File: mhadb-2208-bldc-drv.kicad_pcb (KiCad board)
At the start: 2 copper layers, 45 x 40 mm, 69 parts, among them J1 TC2030, J2 Conn_01x04, J3 Conn_01x04_Pin, M1 Motor_3_Phases, SW1 SW_Push, SW2 SW_Push, SW3 SW_Push, U1 SN65HVD230, U2 STM32F103C8Tx, U3 DRV8311H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

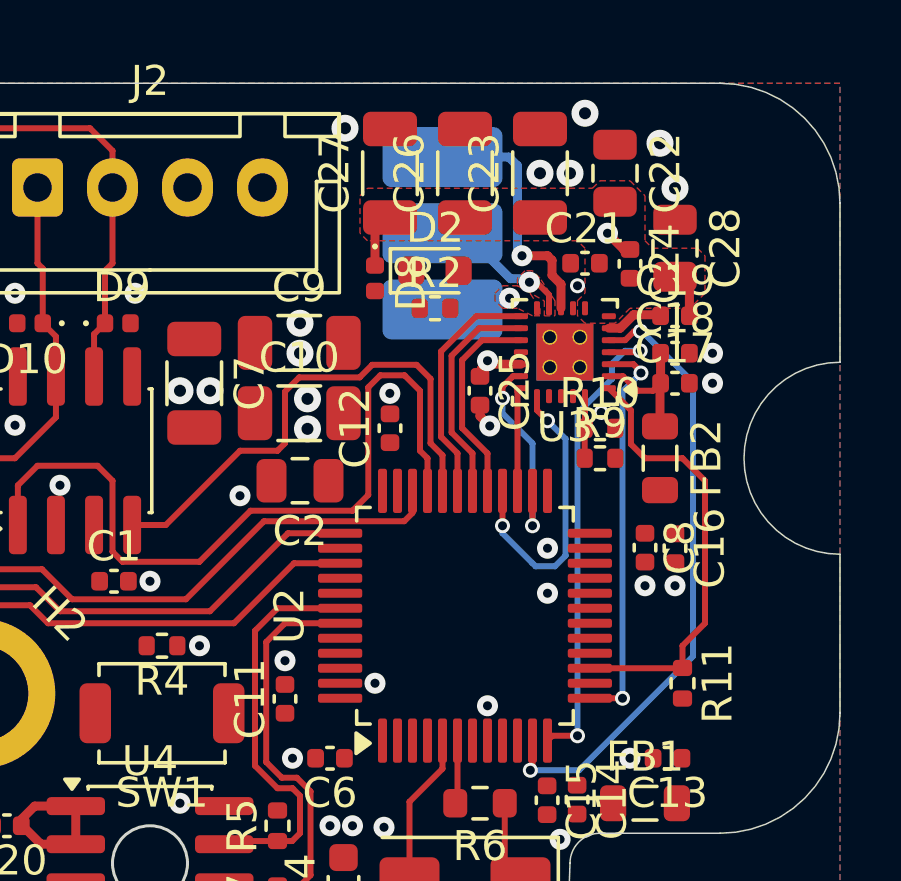
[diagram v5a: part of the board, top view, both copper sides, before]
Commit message: pcb: route +BATT power
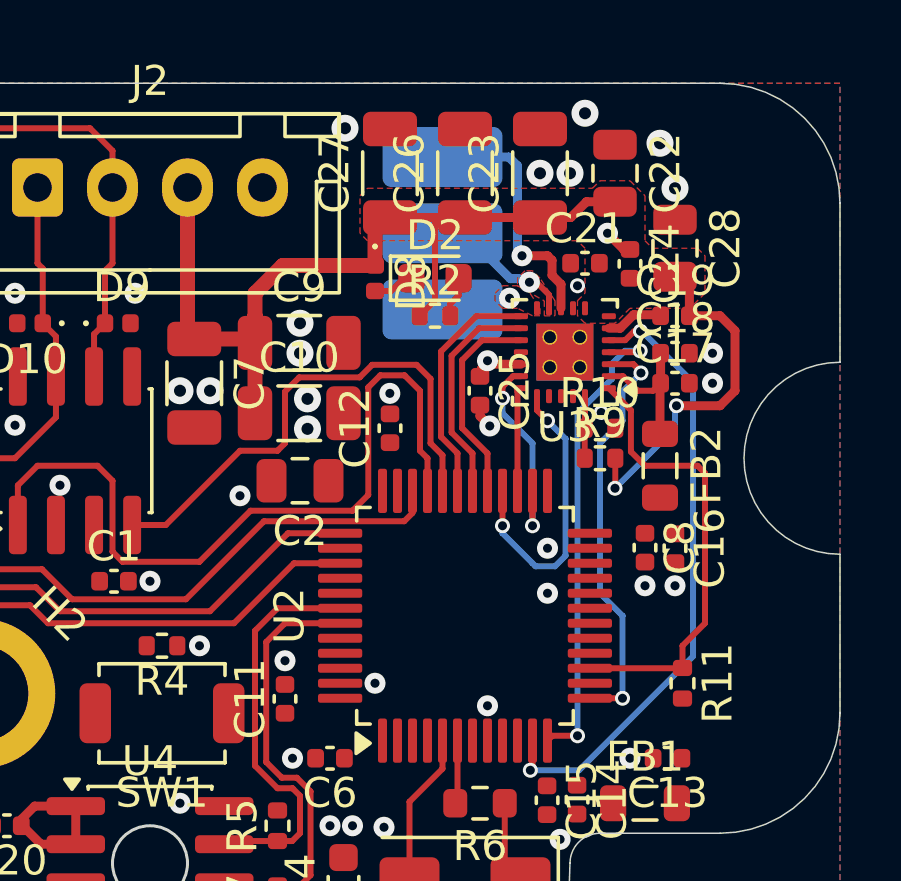
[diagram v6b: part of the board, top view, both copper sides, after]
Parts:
- moved D2 0.25 mm to (128.5, 66.5)
- moved FB2 0.25 mm to (136.0, 72.8)
- moved R2 0.25 mm to (128.5, 67.8)
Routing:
- net +BATT: track 3.31 -> 40.6 mm, vias 0 -> 2
- net GND: track 1.80 -> 3.29 mm
- net Net-(D2-A): track 0.00 -> 1.36 mm
- net /SOC: track 13.4 -> 14.0 mm

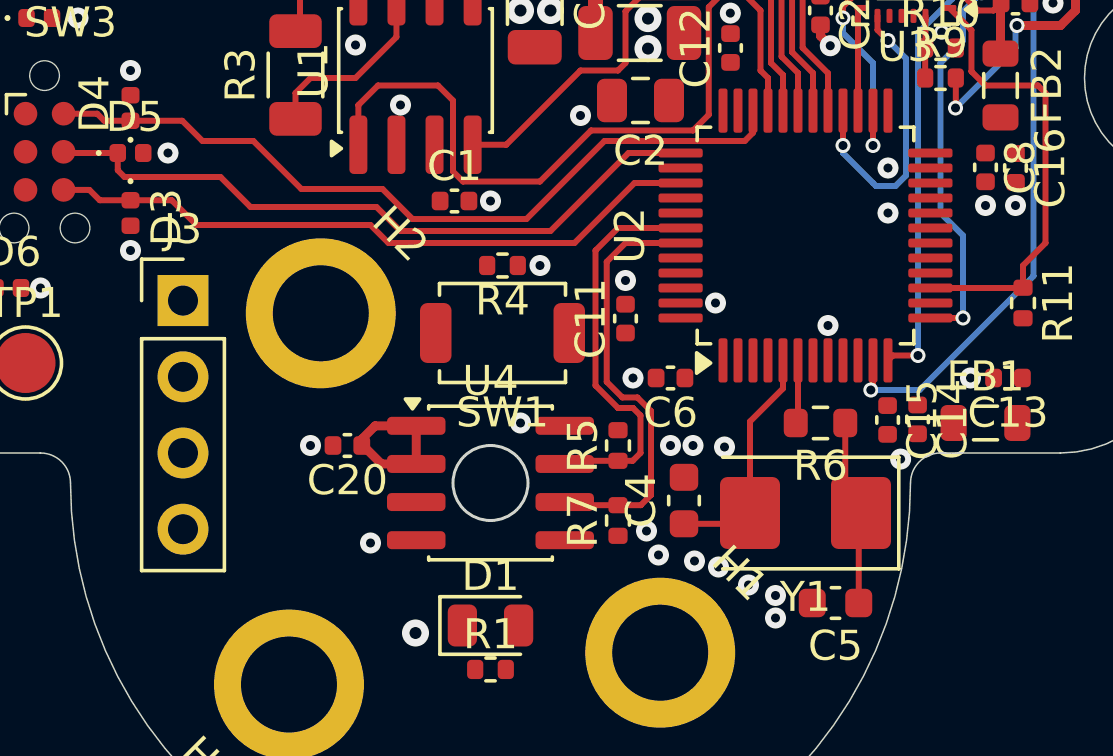
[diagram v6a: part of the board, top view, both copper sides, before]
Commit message: pcb: route spare GPIOs
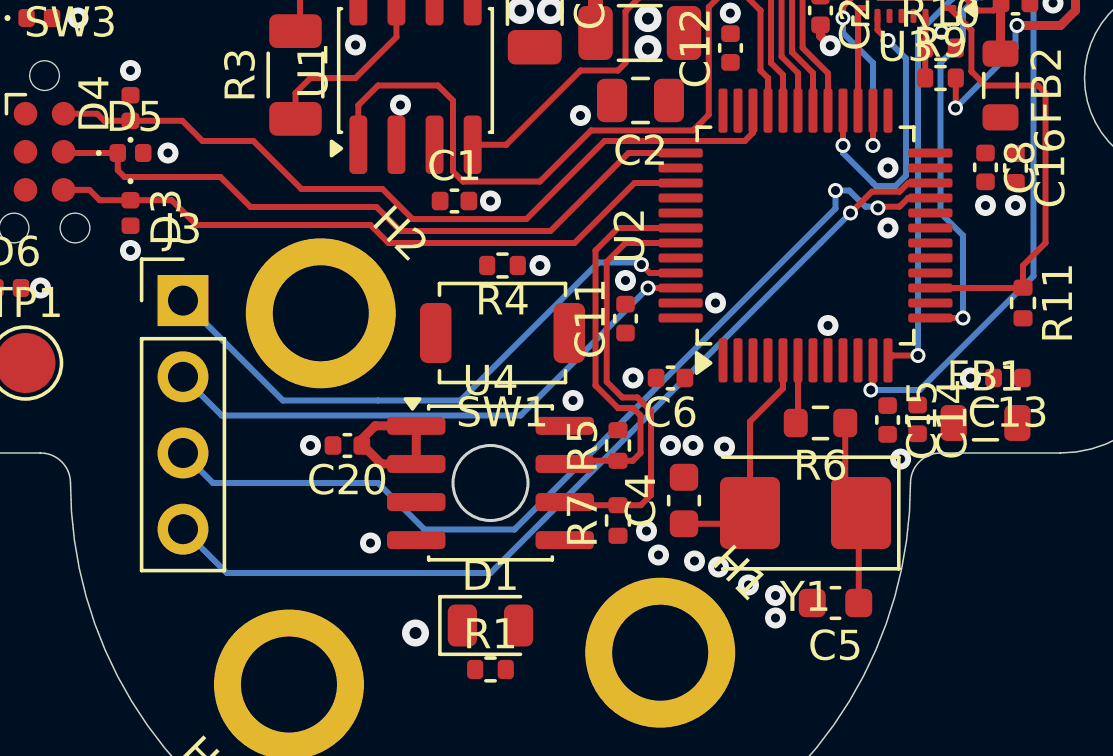
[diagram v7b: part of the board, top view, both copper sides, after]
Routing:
- net Net-(J3-Pin_3): track 0.00 -> 31.4 mm, vias 0 -> 2
- net Net-(J3-Pin_4): track 0.00 -> 30.9 mm, vias 0 -> 1
- net Net-(J3-Pin_1): track 0.00 -> 20.0 mm, vias 0 -> 1
- net Net-(J3-Pin_2): track 0.00 -> 18.9 mm, vias 0 -> 1

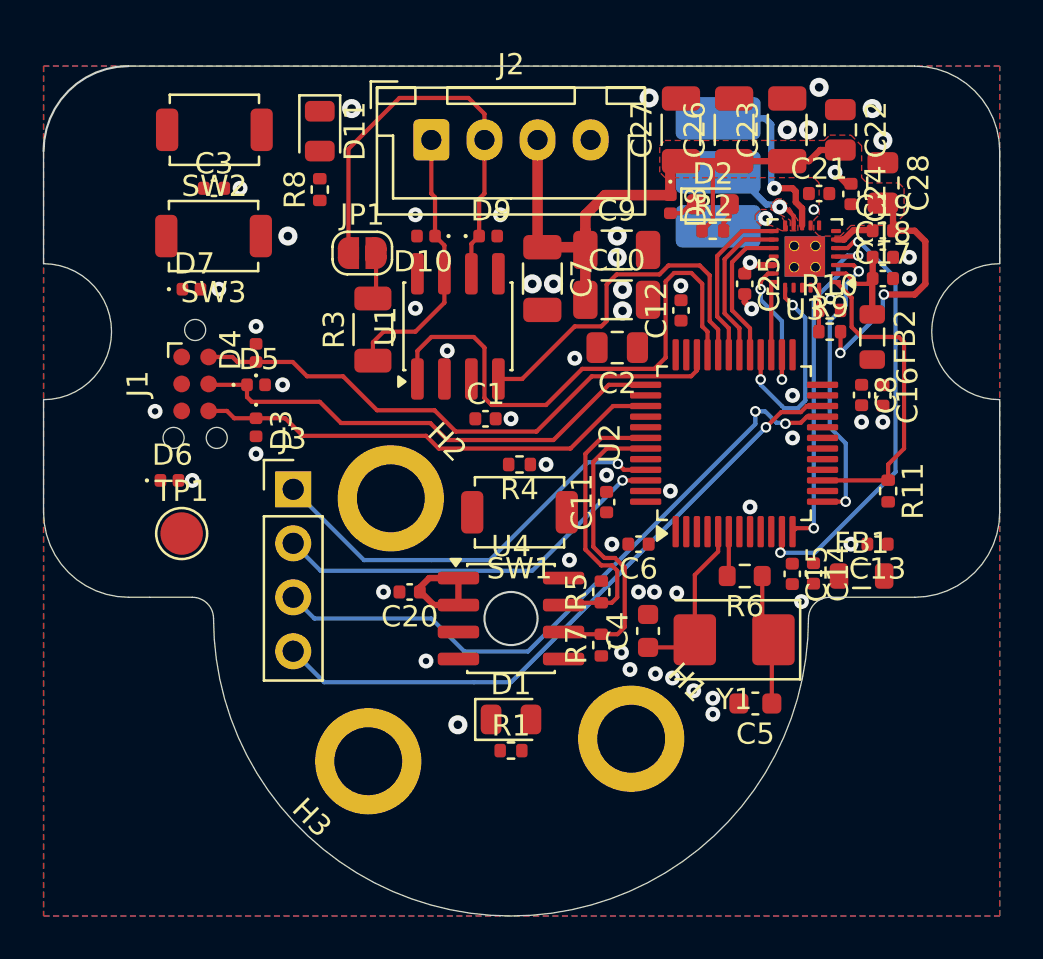
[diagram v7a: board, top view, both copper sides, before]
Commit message: pcb: route +3v3 PWR
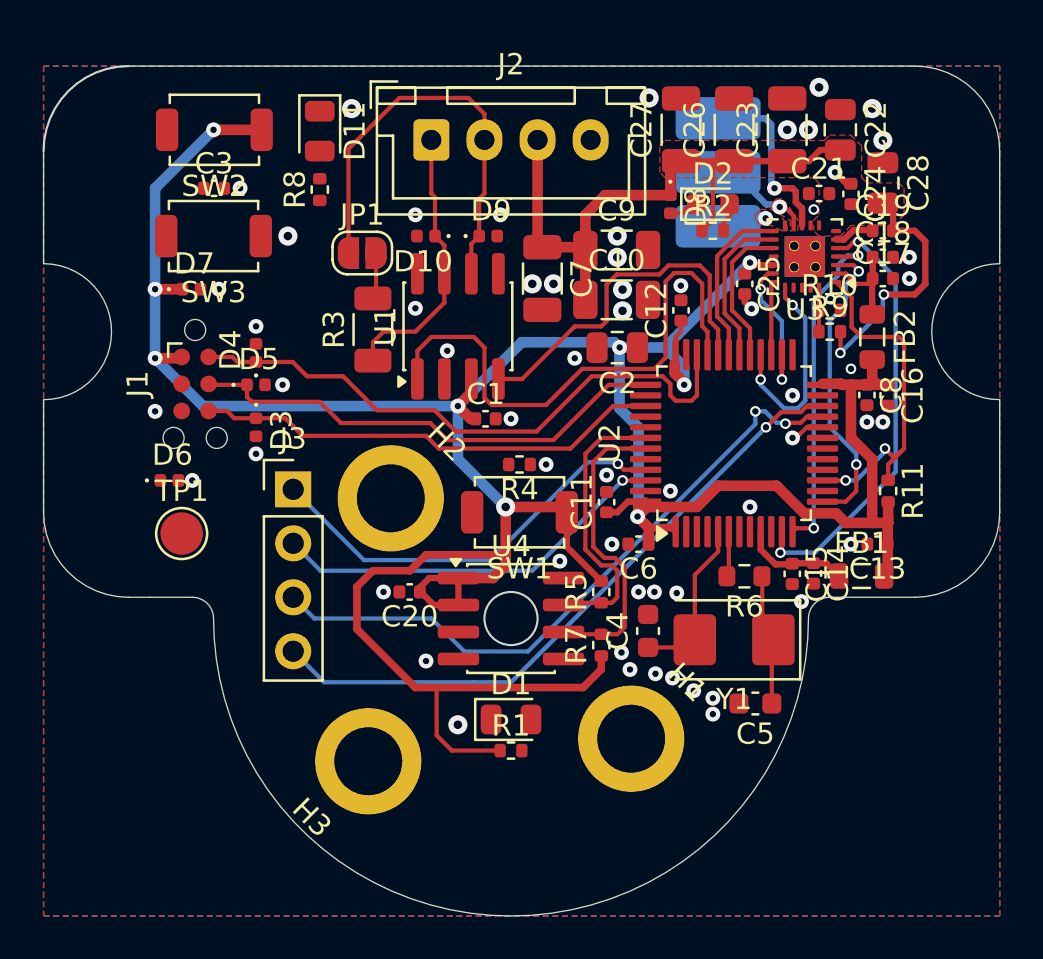
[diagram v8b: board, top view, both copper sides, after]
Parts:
- moved C16 0.25 mm to (136.8, 75.5)
- moved C8 0.25 mm to (135.8, 75.5)
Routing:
- net +3V3: track 7.34 -> 152.4 mm, vias 1 -> 9
- net Net-(U2-VDDA): track 0.00 -> 5.09 mm
- net /SWDIO: track 26.4 -> 28.3 mm
- net /~{FAULT}: track 15.1 -> 16.9 mm, vias 0 -> 2
- net GND: track 3.29 -> 4.91 mm, vias 59 -> 60
